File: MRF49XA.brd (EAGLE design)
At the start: 43 x 31.4 mm, 46 parts, among them J1 AVR_SPI_PRG_6NS, Q1 10Mhz, U1 ATSHA204, U2 ANT1204F002R0433A, U4 MCP73831, Y1 16MHZ

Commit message: PDF
Added PDF of the circuit.
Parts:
- moved C8 0.30 mm to (32.7, 20.3)
- moved C4 0.22 mm to (29.1, 20.0)
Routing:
- net +3V3: track 169.2 -> 167.9 mm
- net D13PWM: track 34.5 -> 33.8 mm

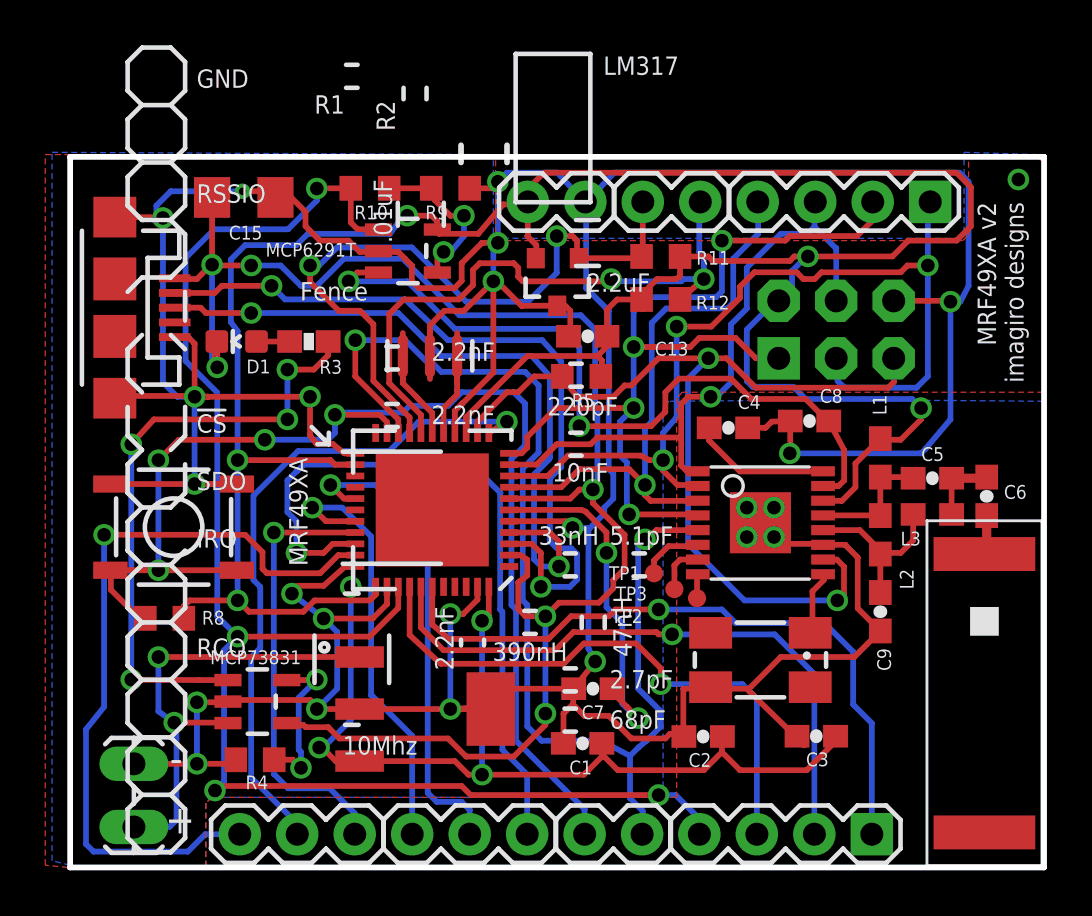
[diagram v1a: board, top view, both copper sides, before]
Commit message: Linear regulator changed
Changed it. Cheaper. Plus the other one would have blown up my circuit.
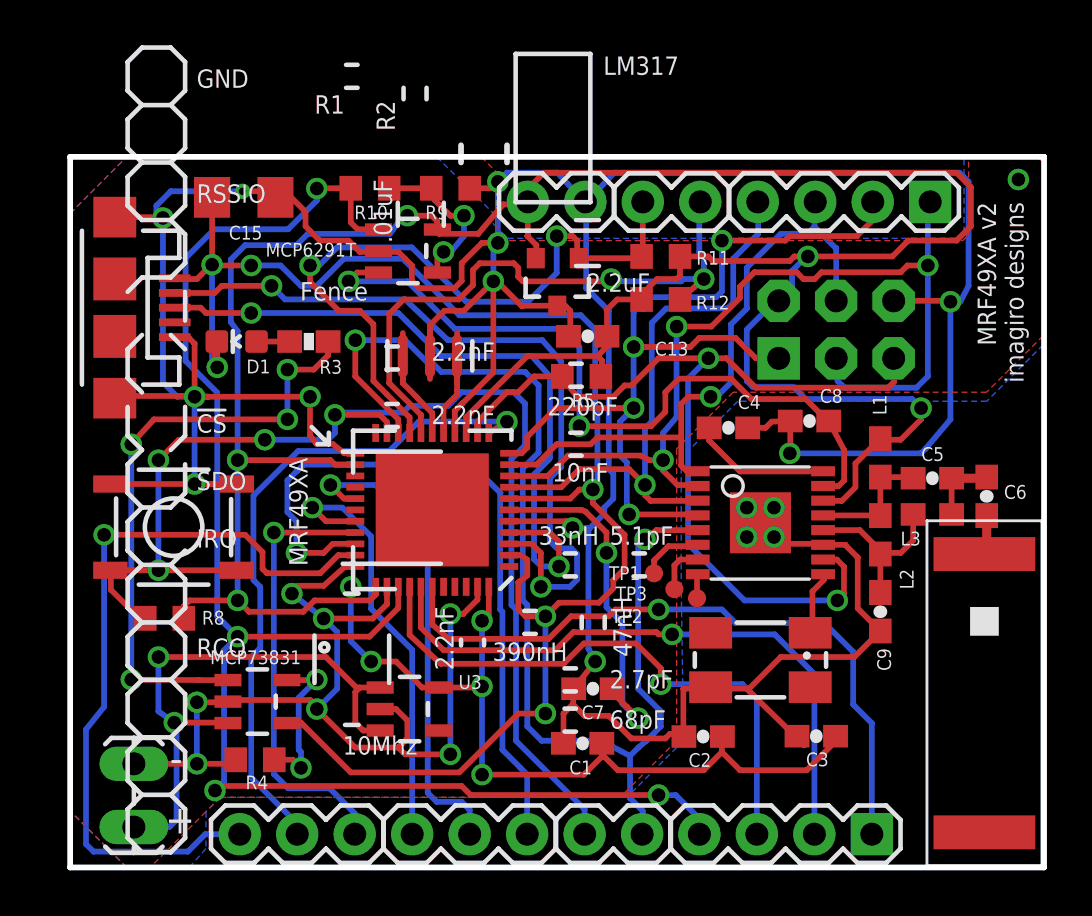
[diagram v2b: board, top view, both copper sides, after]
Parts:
- removed U$4: (no value), TestLibrary:TLV1117
- added U3: V_REG_LDOSMD, SparkFun-PowerIC:SOT23-5
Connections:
- net +3V3: now also U3.5; no longer U$4.P$3
- net GND: now also U3.2; no longer U$4.P$2, U$4.P$4
- net V+: now also U3.1, U3.3; no longer U$4.P$1
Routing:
- net +3V3: track 167.9 -> 161.5 mm, vias 9 -> 10
- net V+: track 20.9 -> 25.2 mm
- net GND: track 232.4 -> 231.0 mm

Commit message: Capacitor and V reg
Added Aref capacitor. Changed voltage regulator.
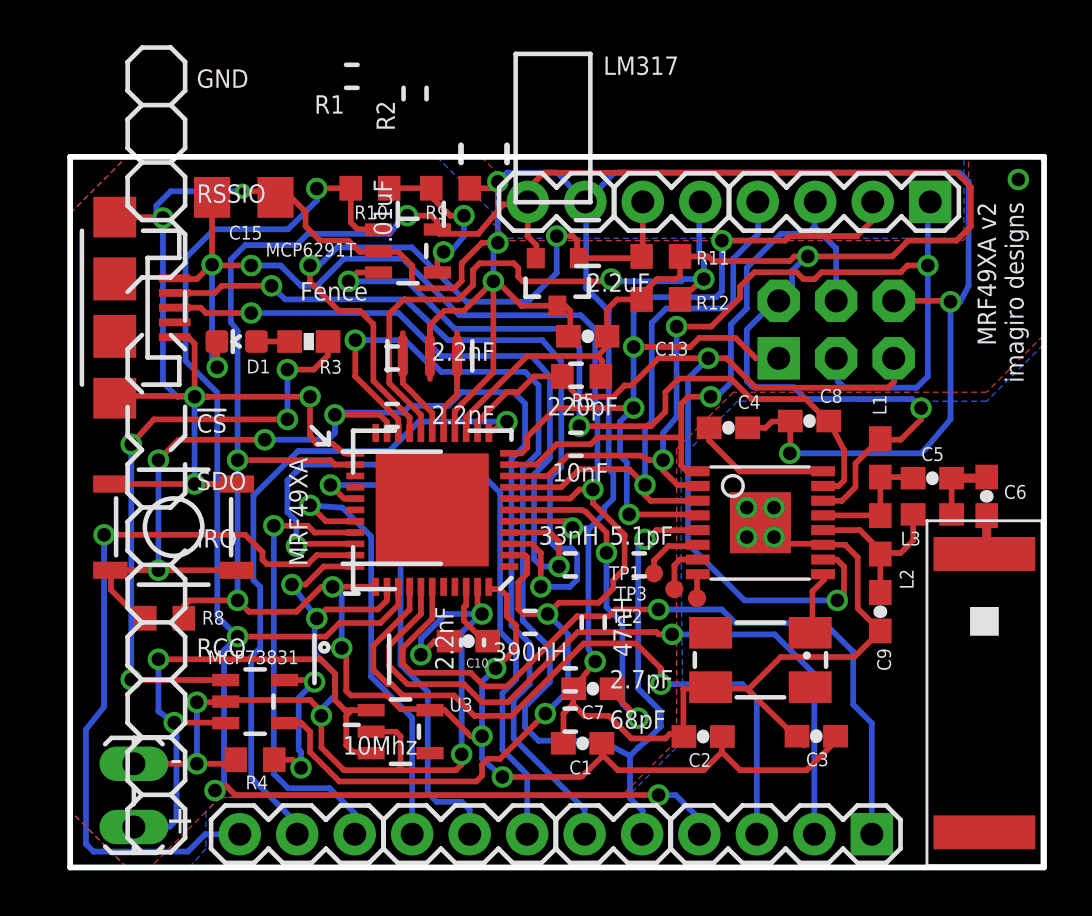
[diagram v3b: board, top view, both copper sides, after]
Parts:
- added C10: 0.1uF, SparkFun-Capacitors:0603-CAP
- moved U3 1.08 mm to (14.6, 6.60)
- moved U4 0.10 mm to (8.17, 7.93)
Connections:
- new net AREF: C10.1, U$3.42
- net GND: now also C10.2
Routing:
- net GND: track 231.0 -> 238.8 mm, vias 19 -> 20
- net A1: track 25.8 -> 31.0 mm
- net A2: track 27.8 -> 32.7 mm
- net A3: track 30.2 -> 34.8 mm
- net AREF: track 0.00 -> 3.27 mm
- net +3V3: track 161.5 -> 164.3 mm
- net VBUS: track 73.9 -> 76.1 mm
- net INT2: track 51.1 -> 52.1 mm
- net V+: track 25.2 -> 25.9 mm
- net INT1: track 55.1 -> 55.7 mm
- net D13PWM: track 33.8 -> 33.2 mm
